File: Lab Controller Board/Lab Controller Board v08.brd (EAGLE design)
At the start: 50 x 50 mm, 48 parts, among them Q2 MMBT5088, Q3 100A/100V, Q4 MMBT5088, Q5 100A/100V, Q6 MMBT5088, Q7 100A/100V, Q8 MMBT5088, U1 ATMEGA328P_TQFP, U2 CH340G, U3 +12v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

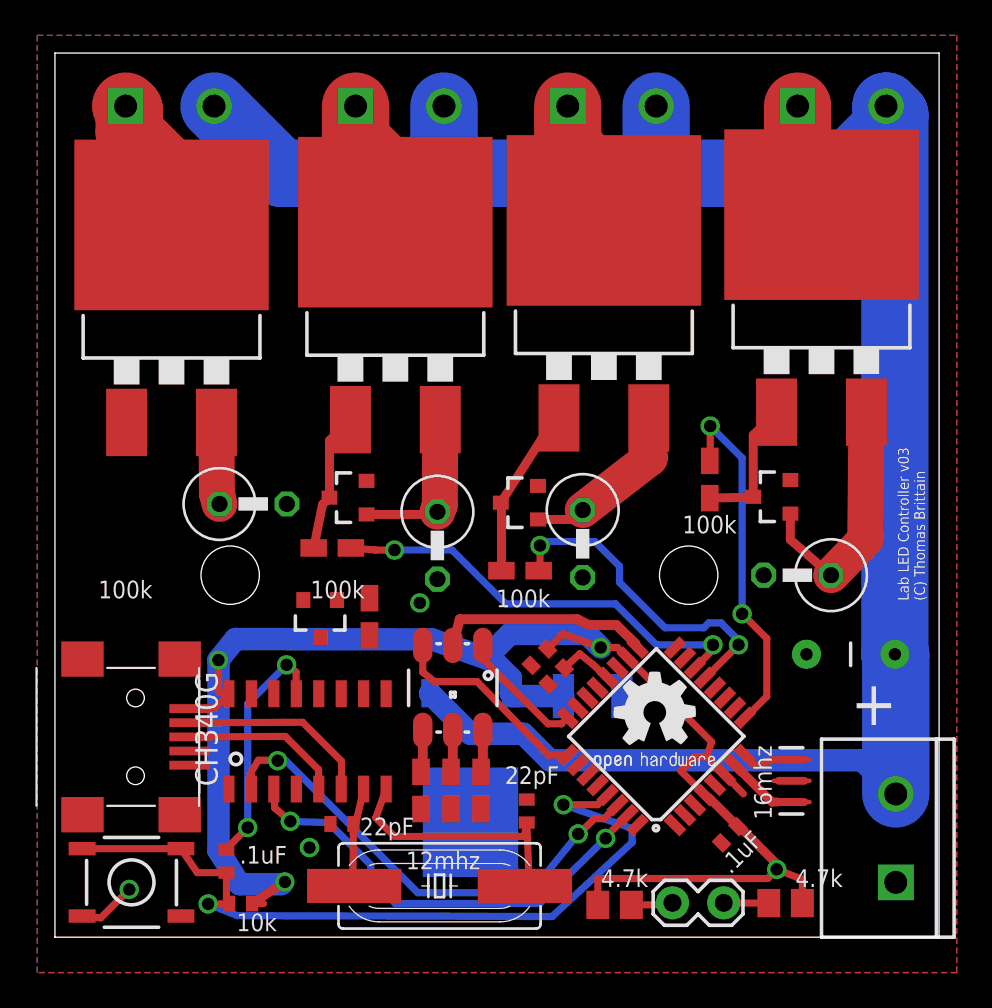
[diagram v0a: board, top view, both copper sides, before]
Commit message: Added ESP-07, RX/TX level converter, temp probe connection.  Cleaned silkscreen
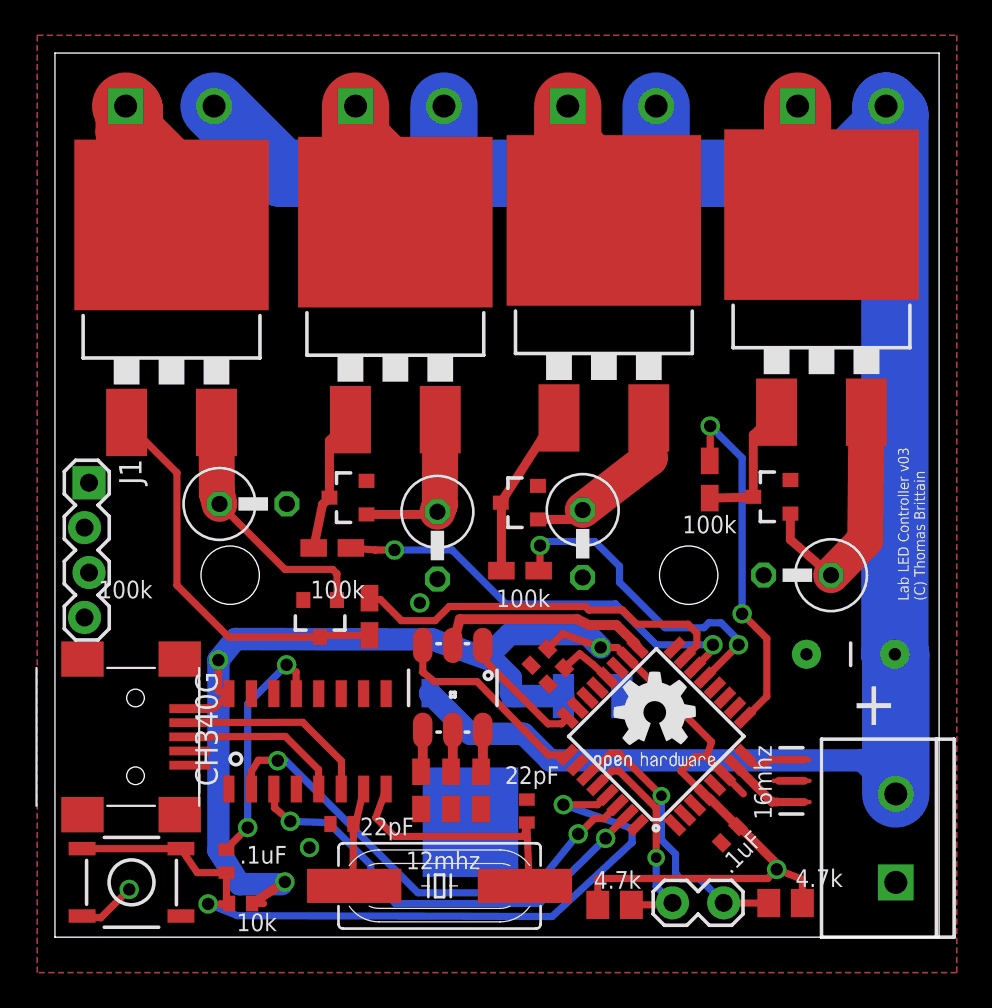
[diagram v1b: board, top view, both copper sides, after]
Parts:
- added J1: (no value), SparkFun-Connectors:1X04_LOCK
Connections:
- net 2: now also J1.3
- net 3: now also J1.2
- net GND: now also J1.1
- net VCC: now also J1.4
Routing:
- net PWM_B1: track 0.97 -> 23.5 mm
- net 11: track 0.00 -> 21.7 mm
- net SDA: track 2.55 -> 16.4 mm, vias 0 -> 1
- net SCL: track 2.37 -> 12.6 mm, vias 0 -> 1
- net FET_SOURCE1: track 5.11 -> 14.9 mm
